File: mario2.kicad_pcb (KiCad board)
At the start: 2 copper layers, 38.1 x 40.6 mm, 7 parts, among them J1 Resistors, J2 FSRs, U1 Teensy-LC

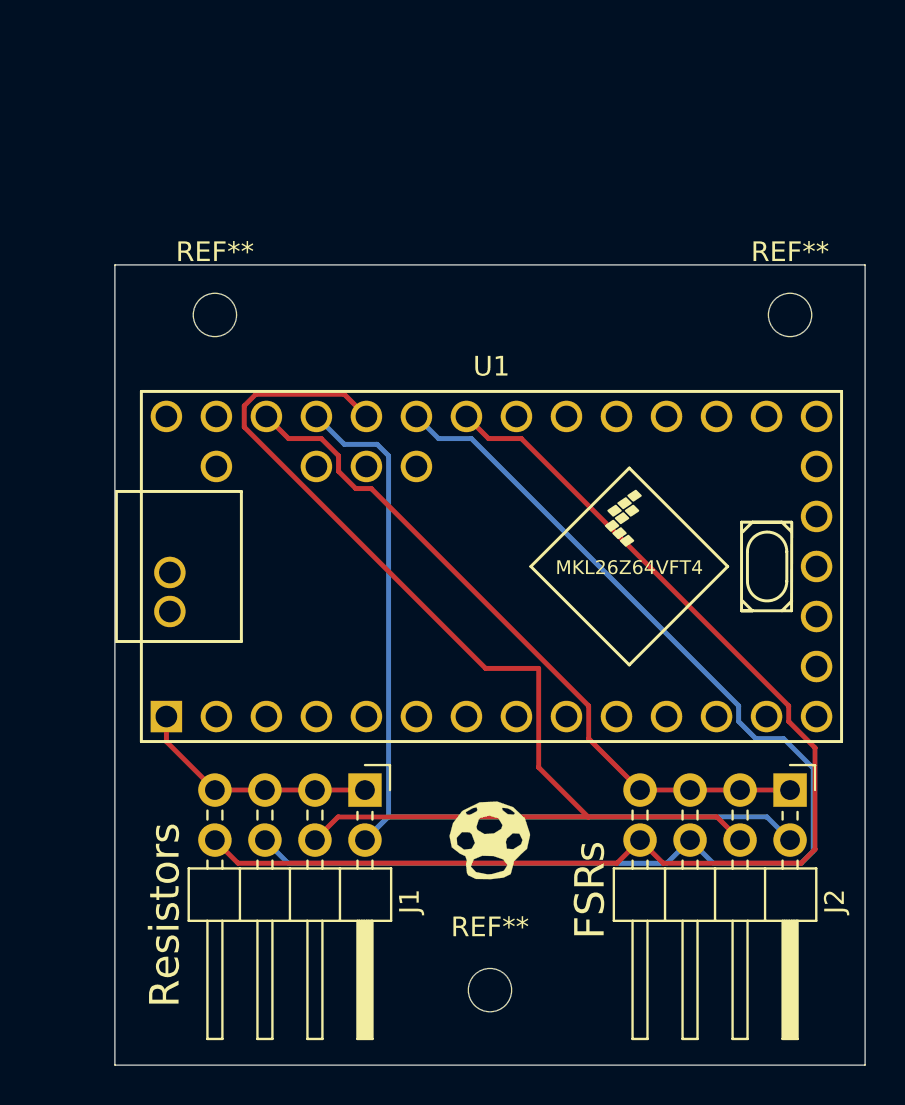
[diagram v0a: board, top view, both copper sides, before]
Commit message: direct solder resistors
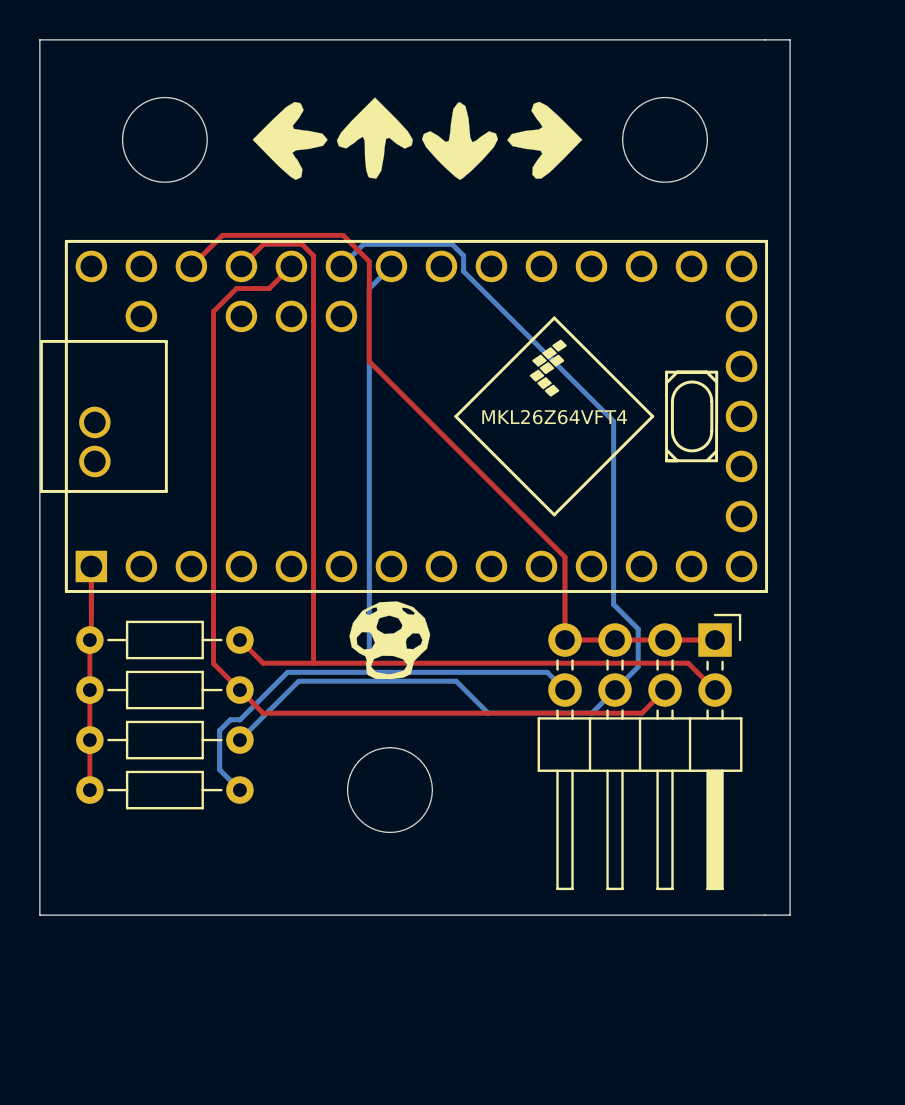
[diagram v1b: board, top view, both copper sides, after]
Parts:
- removed J1: Resistors, pin headers:PinHeader_2x04_P2.54mm_Horizontal
- removed the REF** at (106.7, 99.1)
- removed the REF** at (121.9, 64.8)
- removed the REF** at (92.7, 64.8)
- added G***: LOGO, mario2:arrows, F.Cu at (102.9, 55.9)
- added R1: R, Resistor_THT:R_Axial_DIN0204_L3.6mm_D1.6mm_P7.62mm_Horizontal, F.Cu at (94.0, 81.3)
- added R2: R, Resistor_THT:R_Axial_DIN0204_L3.6mm_D1.6mm_P7.62mm_Horizontal, F.Cu at (94.0, 83.8)
- added R3: R, Resistor_THT:R_Axial_DIN0204_L3.6mm_D1.6mm_P7.62mm_Horizontal, F.Cu at (94.0, 86.4)
- added R4: R, Resistor_THT:R_Axial_DIN0204_L3.6mm_D1.6mm_P7.62mm_Horizontal, F.Cu at (94.0, 88.9)
- added REF**: MountingHole_4.3mm_M4, MountingHole:MountingHole_4.3mm_M4, F.Cu at (101.6, 88.9)
- added REF**: MountingHole_4.3mm_M4, MountingHole:MountingHole_4.3mm_M4, F.Cu at (115.6, 55.9)
- added REF**: MountingHole_4.3mm_M4, MountingHole:MountingHole_4.3mm_M4, F.Cu at (90.2, 55.9)
- moved G*** 11.4 mm to (101.6, 81.3)
- moved J2 8.52 mm to (118.1, 81.3)
- moved U1 8.52 mm to (102.9, 69.9)
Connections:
- net Net-(J1-Pad2) renamed /FSR_4
- net Net-(J1-Pad4) renamed /FSR_3
- net Net-(J1-Pad6) renamed /FSR_2
- net Net-(J1-Pad8) renamed /FSR_1
- net Net-(J2-Pad1) renamed /3.3v
- U1 pad 1: Net-(J1-Pad1) -> /GND
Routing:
- net /FSR_1: track 62.5 -> 43.7 mm
- net /GND: track 0.00 -> 13.8 mm
- net Net-(J1-Pad1): track 12.4 -> 0.00 mm
- net /FSR_3: track 59.2 -> 48.5 mm
- net /FSR_2: track 61.8 -> 54.6 mm
- net /3.3v: track 35.9 -> 41.2 mm
- net /FSR_4: track 47.1 -> 50.3 mm
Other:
- board size 38.1 x 40.6 mm -> 38.1 x 44.5 mm
- board text added: "MAR.IO 2 made with <3 by bandit zaniel iamevn widget joshhead"
- board text added: "staminanation.com"
- board text removed: "FSRs"
- board text removed: "MAR.IO 2"
- board text removed: "Resistors"
- board text removed: "made with <3 by bandit, zaniel, and iamevn"

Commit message: clean up wires
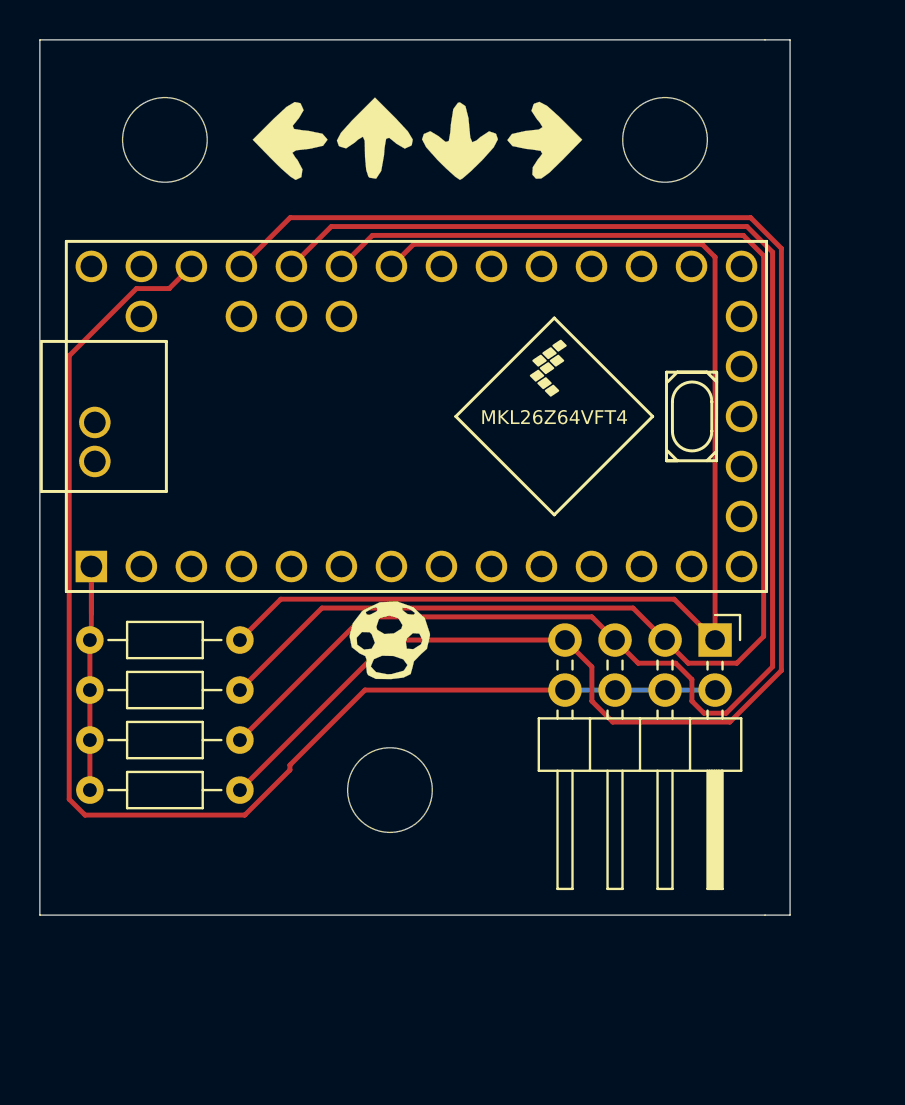
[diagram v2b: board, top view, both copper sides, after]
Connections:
- J2 pad 1: /3.3v -> /FSR_4
- J2 pad 2: /FSR_4 -> /3.3v
- J2 pad 3: /3.3v -> /FSR_3
- J2 pad 4: /FSR_3 -> /3.3v
- J2 pad 5: /3.3v -> /FSR_2
- J2 pad 6: /FSR_2 -> /3.3v
- J2 pad 7: /3.3v -> /FSR_1
- J2 pad 8: /FSR_1 -> /3.3v
- U1 pad 27: /FSR_1 -> /FSR_4
- U1 pad 28: /FSR_2 -> /FSR_3
- U1 pad 29: /FSR_3 -> /FSR_2
- U1 pad 30: /FSR_4 -> /FSR_1
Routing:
- net /FSR_1: track 43.7 -> 85.0 mm
- net /FSR_2: track 54.6 -> 80.2 mm
- net /3.3v: track 41.2 -> 66.5 mm
- net /FSR_3: track 48.5 -> 71.9 mm
- net /FSR_4: track 50.3 -> 62.5 mm
